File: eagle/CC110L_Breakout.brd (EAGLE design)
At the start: 20.9 x 30.9 mm, 28 parts

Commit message: almost completed board
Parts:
- added LOGO1: OSHW-LOGOS, SparkFun-Aesthetics:OSHW-LOGO-S
- moved C127 2.30 mm to (10.5, 23.5)
- moved C126 2.30 mm to (10.4, 25.8)
- moved C81 0.70 mm to (15.6, 13.3)
- moved C91 0.54 mm to (13.1, 11.8)
- moved C41 0.36 mm to (8.90, 6.20)
- moved C51 0.36 mm to (10.2, 6.20)
- moved C101 0.30 mm to (15.6, 8.60)
- moved C122 0.20 mm to (9.60, 20.8)
- moved L132 0.20 mm to (7.10, 20.8)
- moved L125 0.17 mm to (12.6, 24.6), turned to 270 degrees
- moved C123 0.10 mm to (6.20, 23.4), turned to 0 degrees
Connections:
- net GDO0: now also JP1.6; no longer JP1.7
- net GDO2: now also JP1.5; no longer JP1.6
- net MISO: now also JP1.4; no longer JP1.3
- net RF_CS: now also JP1.7; no longer JP1.5
- net SCK: now also JP1.3; no longer JP1.4
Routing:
- net VCC: track 0.00 -> 70.7 mm, vias 0 -> 7
- net GDO2: track 0.00 -> 12.7 mm
- net RF_CS: track 0.00 -> 11.7 mm
- net N$12: track 0.00 -> 11.4 mm
- net MISO: track 0.00 -> 11.1 mm
- net GDO0: track 0.00 -> 10.3 mm
- net MOSI: track 0.00 -> 9.73 mm
- net SCK: track 0.00 -> 9.38 mm
- net N$13: track 0.00 -> 9.00 mm
- net N$5: track 0.00 -> 4.39 mm
- net N$2: track 0.00 -> 4.35 mm
- net N$11: track 0.00 -> 4.13 mm
- net N$8: track 0.00 -> 2.84 mm
- net N$7: track 0.00 -> 2.83 mm
- net N$16: track 0.00 -> 2.74 mm
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- added copper zone on layer 1, net GND
- added copper zone on layer 16, net GND
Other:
- board size 20.9 x 30.9 mm -> 21 x 31 mm
- board text added: "..."
- board text added: "CS"
- board text added: "GDO0"
- board text added: "GDO2"
- board text added: "GND"
- board text added: "Idle Hands Development"
- board text added: "SCK"
- board text added: "SI"
- board text added: "SO"
- board text added: "VCC"

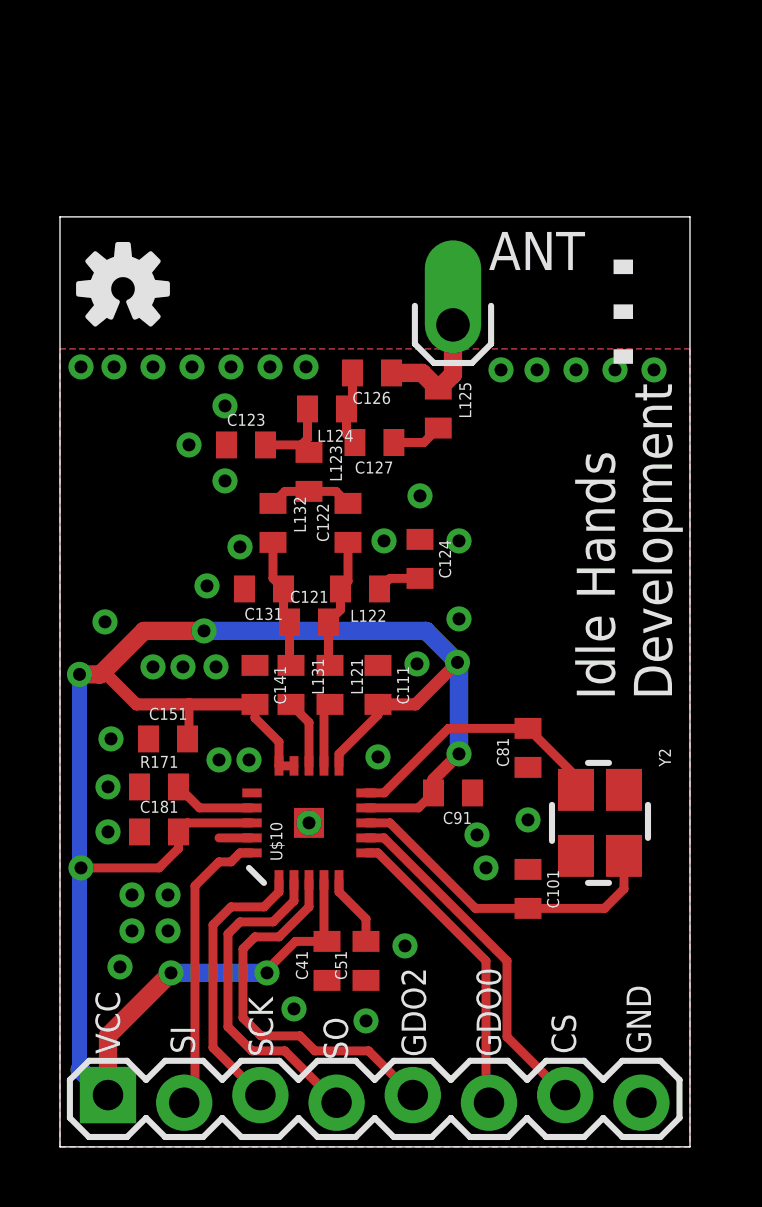
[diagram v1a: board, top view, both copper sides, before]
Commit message: Finilized and uploaded to OSHpark ordered
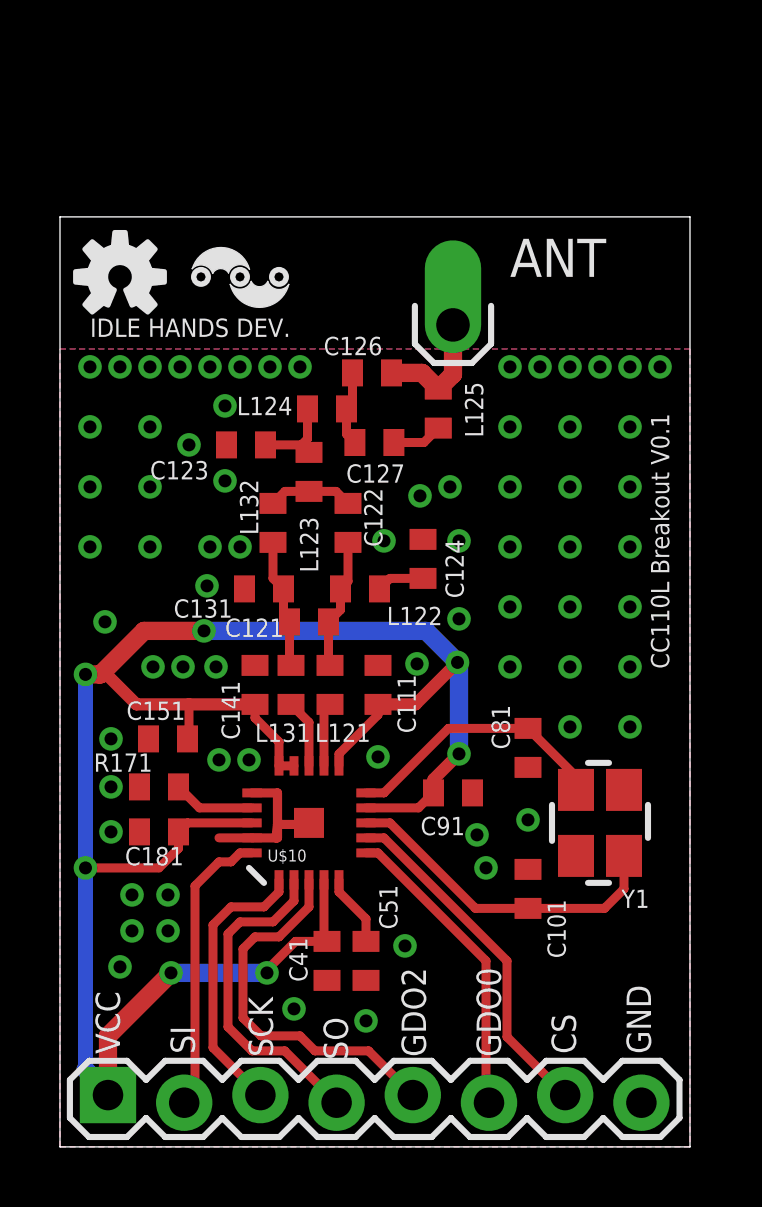
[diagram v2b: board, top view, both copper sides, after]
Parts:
- added LOGO2: IDLEHANDS_LOGOS, IdleHandsProject:IHD-LOGO-S
- moved LOGO1 0.41 mm to (2.00, 29.0)
- moved C124 0.10 mm to (12.1, 19.6)
- renumbered Y2 to Y1
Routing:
- net GND: track 1.10 -> 5.85 mm, vias 44 -> 70
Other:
- board text added: "CC110L Breakout V0.1"
- board text added: "IDLE HANDS DEV."
- board text removed: "..."
- board text removed: "Idle Hands Development"
